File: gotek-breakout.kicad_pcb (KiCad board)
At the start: 2 copper layers, 100 x 70 mm, 13 parts, among them J1 FFC 10x1 0.5mm, J11 FFC 10x1 0.5mm, J12 Gotek 6-pin connector, J13 USB Breakout, J14 USB_B_Micro, J2 USB_A, J3 OLED, J4 Encoder

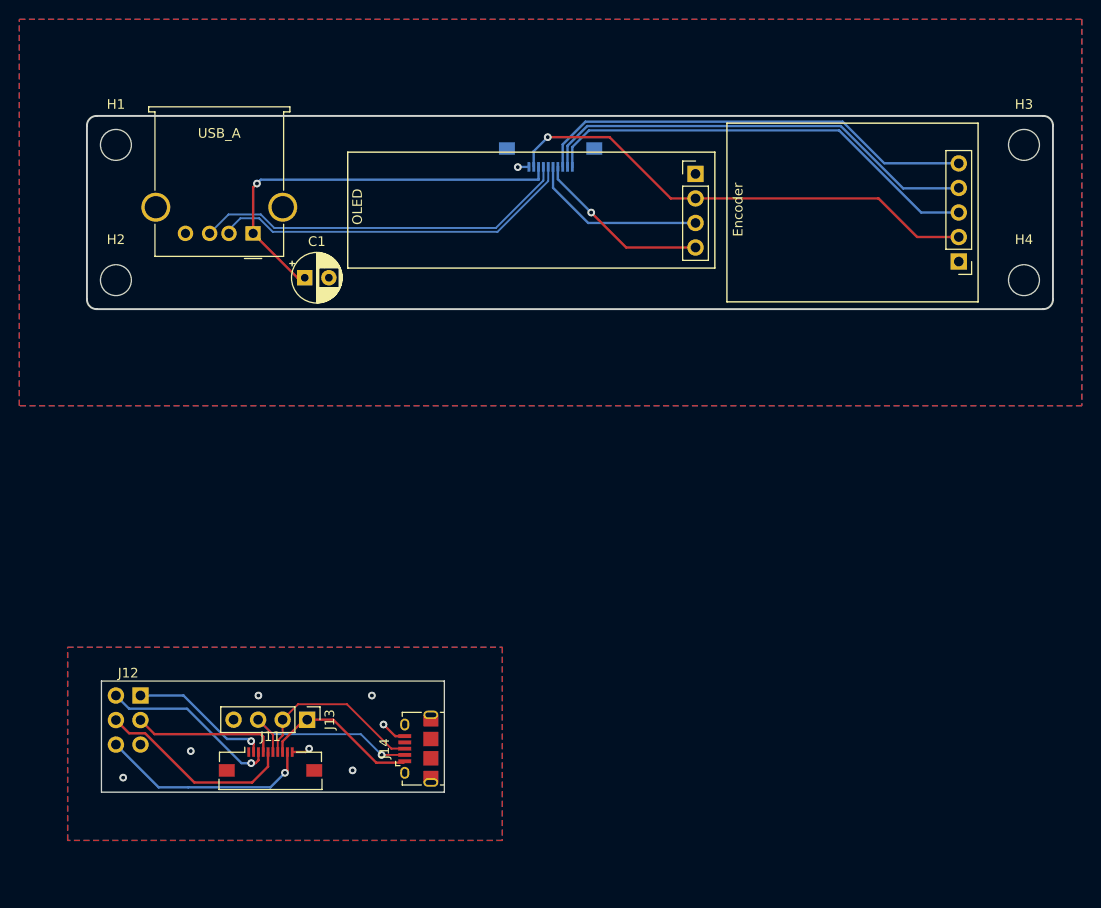
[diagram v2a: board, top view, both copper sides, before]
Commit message: Breakout board only for newer goteks
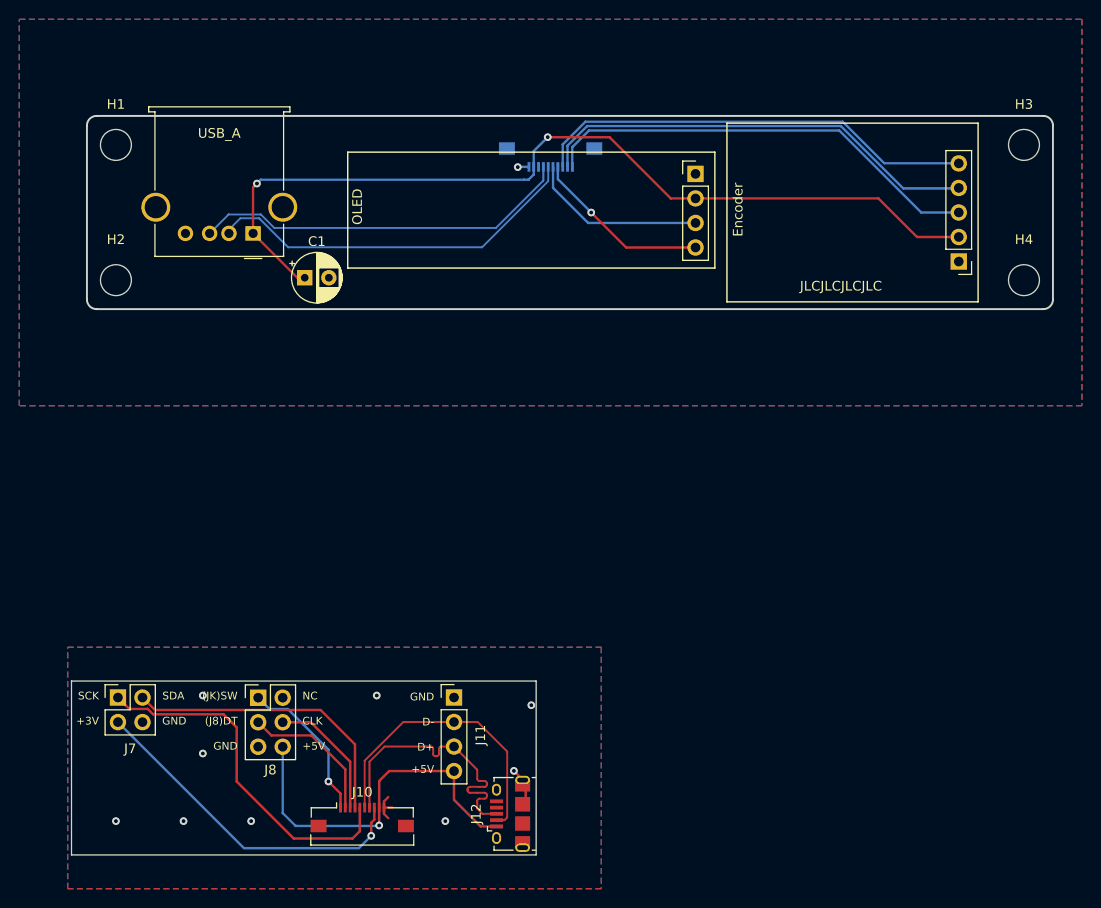
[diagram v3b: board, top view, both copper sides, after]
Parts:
- removed J13: USB Breakout, Connector_PinHeader_2.54mm:PinHeader_1x04_P2.54mm_Vertical
- removed J14: USB_B_Micro, Connector_USB:USB_Micro-B_Amphenol_10118194_Horizontal
- added J10: FFC 10x1 0.5mm, Connector_FFC-FPC:Molex_54548-1071_1x10-1MP_P0.5mm_Horizontal, F.Cu at (75.5, 112.6)
- added J7: J7 Right Angle Connector, Connector_PinHeader_2.54mm:PinHeader_2x02_P2.54mm_Vertical, F.Cu at (50.2, 100.2)
- added J8: J8 Mirror, Connector_PinHeader_2.54mm:PinHeader_2x03_P2.54mm_Vertical, F.Cu at (64.7, 100.2)
- J11: value FFC 10x1 0.5mm -> USB Breakout; footprint Connector_FFC-FPC:Molex_54548-1071_1x10-1MP_P0.5mm_Horizontal -> Connector_PinHeader_2.54mm:PinHeader_1x04_P2.54mm_Vertical
- J12: value Gotek 6-pin connector -> USB Micro; footprint Connector_PinHeader_2.54mm:PinHeader_2x03_P2.54mm_Vertical -> Connector_USB:USB_Micro-B_Amphenol_10118194_Horizontal
- moved J12 42.6 mm to (90.8, 112.2), turned to 90 degrees
- moved J11 20.1 mm to (85.0, 100.2)
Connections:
- C1 pad 1: /USB_VIN -> /+5V
- J1 pad 2: /VCC -> /+5V
- J1 pad 3: /USB_VIN -> /+3V
- J11 pad 1: /Gotek Side/ROT_SW -> /Gotek Side/GND
- J11 pad 2: /Gotek Side/ROT_DT -> /Gotek Side/USB_D-
- J11 pad 3: /Gotek Side/ROT_CLK -> /Gotek Side/USB_D+
- J11 pad 4: /Gotek Side/OLED_SDA -> /Gotek Side/+5V
- J12 pad 1: /Gotek Side/ROT_DT -> /Gotek Side/+5V
- J12 pad 2: /Gotek Side/OLED_SDA -> /Gotek Side/USB_D-
- J12 pad 3: /Gotek Side/GND -> /Gotek Side/USB_D+
- J12 pad 4: /Gotek Side/VCC -> unconnected-(J12-ID-Pad4)
- J12 pad 5: /Gotek Side/OLED_SCK -> /Gotek Side/GND
- J12 pad 6: /Gotek Side/ROT_CLK -> /Gotek Side/GND
- J2 pad 1: /USB_VIN -> /+5V
- J3 pad 2: /VCC -> /+5V
- J4 pad 2: /VCC -> /+5V
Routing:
- net /+5V: track 0.00 -> 92.9 mm, vias 0 -> 2
- net /VCC: track 50.5 -> 0.00 mm, vias 1 -> 0
- net /USB_VIN: track 43.2 -> 0.00 mm, vias 1 -> 0
- net /Gotek Side/+5V: track 0.00 -> 38.7 mm, vias 0 -> 1
- net /Gotek Side/+3V: track 0.00 -> 35.2 mm, vias 0 -> 1
- net /Gotek Side/VCC: track 22.2 -> 0.00 mm, vias 1 -> 0
- net /Gotek Side/USB_VIN: track 16.6 -> 0.00 mm
- net /Gotek Side/OLED_SCK: track 20.6 -> 37.1 mm
- net /Gotek Side/ROT_SW: track 0.00 -> 16.0 mm, vias 0 -> 1
- net /Gotek Side/OLED_SDA: track 15.0 -> 30.6 mm
- net /Gotek Side/USB_D+: track 18.8 -> 30.4 mm
- net /Gotek Side/USB_D-: track 20.7 -> 30.6 mm, vias 1 -> 0
- net /Gotek Side/ROT_CLK: track 18.6 -> 13.4 mm, vias 1 -> 0
- net /Gotek Side/GND: track 4.59 -> 7.08 mm, vias 7 -> 9
- net /USB_D-: track 38.1 -> 39.5 mm
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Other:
- board size 100 x 70 mm -> 101.6 x 76.5 mm
- board text added: "(J8)DT"
- board text added: "(JK)SW"
- board text added: "+3V"
- board text added: "+5V"
- board text added: "CLK"
- board text added: "D+"
- board text added: "D-"
- board text added: "GND"
- board text added: "JLCJLCJLCJLC"
- board text added: "NC"
- board text added: "SCK"
- board text added: "SDA"
